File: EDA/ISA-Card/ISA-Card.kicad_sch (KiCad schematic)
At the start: 50 parts, among them U7101 74HCT245, U7102 74HCT244, U7104 74HCT138, U7105 74HCT138, U7106 74LS08, U7107 74LS32, U7108 74LS32, U7109 74HC368, U7110 74HC04, U7111 74HC125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

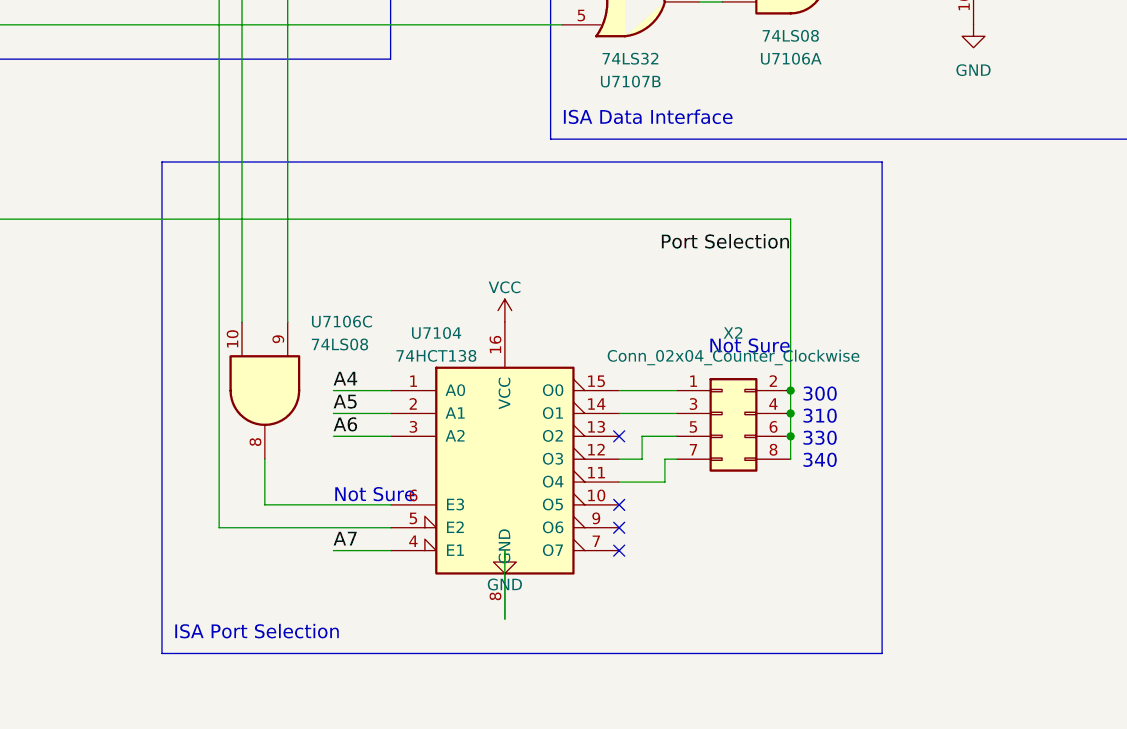
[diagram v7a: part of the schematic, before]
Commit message: Mark default port on schematic
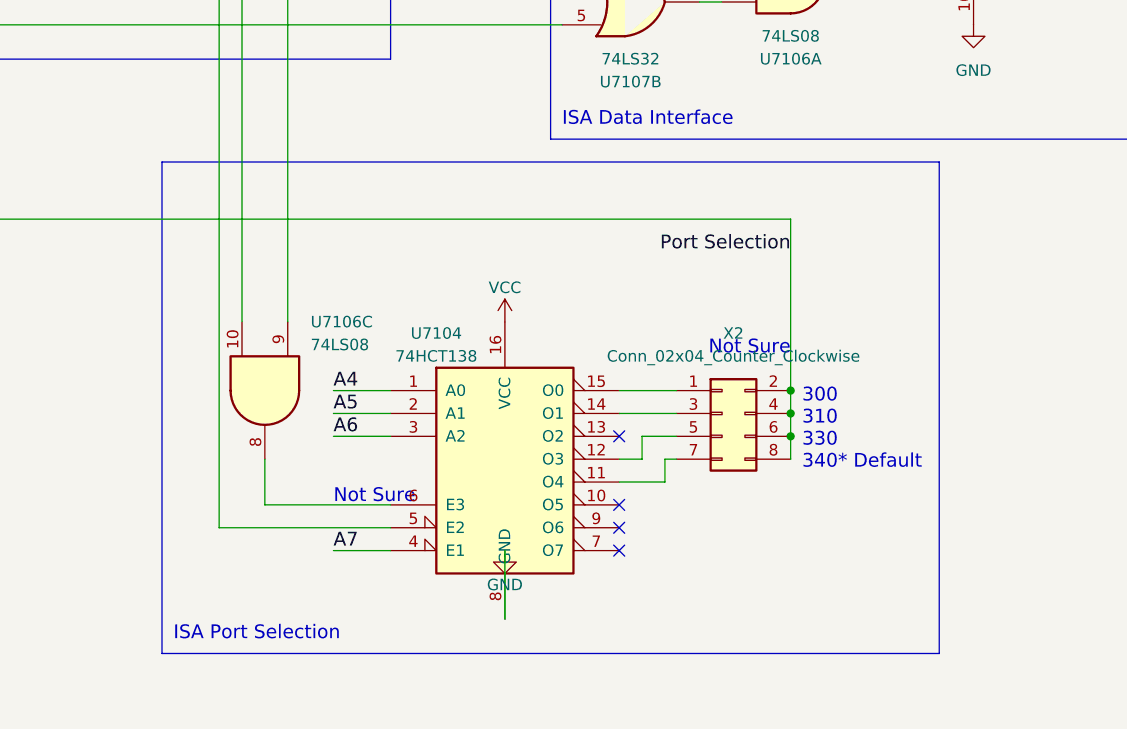
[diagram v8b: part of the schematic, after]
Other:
- note added: "300 310 330 340* Default"
- note removed: "300 310 330 340"
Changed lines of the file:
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@@
     (stroke (width 0) (type default) (color 0 0 0 0))
   )
-  (polyline (pts (xy 383.54 411.48) (xy 383.54 356.87))
+  (polyline (pts (xy 389.89 411.48) (xy 389.89 356.87))
     (stroke (width 0) (type default) (color 0 0 0 0))
   )
@@
     (stroke (width 0) (type default) (color 0 0 0 0))
   )
-  (polyline (pts (xy 303.53 356.87) (xy 383.54 356.87))
+  (polyline (pts (xy 303.53 356.87) (xy 389.89 356.87))
     (stroke (width 0) (type default) (color 0 0 0 0))
   )
@@
     (stroke (width 0) (type default) (color 0 0 0 0))
   )
-  (polyline (pts (xy 303.53 411.48) (xy 383.54 411.48))
+  (polyline (pts (xy 303.53 411.48) (xy 389.89 411.48))
     (stroke (width 0) (type default) (color 0 0 0 0))
   )
@@
     (effects (font (size 1.524 1.524)) (justify right bottom))
   )
-  (text "300\n310\n330\n340" (at 374.65 391.16 0)
+  (text "300\n310\n330\n340* Default" (at 374.65 391.16 0)
     (effects (font (size 1.524 1.524)) (justify left bottom))
   )
